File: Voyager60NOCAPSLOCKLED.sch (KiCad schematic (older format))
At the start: 262 parts, among them Q1 2N7002, SW1 5.2x5.2mm, U1 ATmega32U4-MU, U2 PRTR5V0U2X, Y1 16Mhz

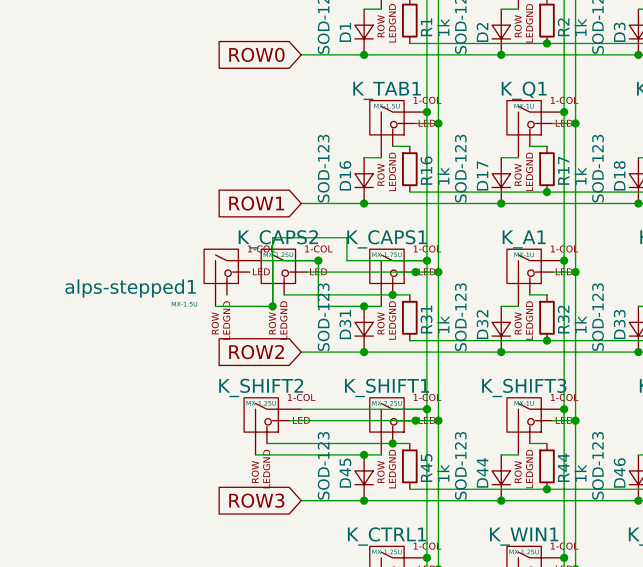
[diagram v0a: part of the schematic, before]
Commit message: Alps Stepped Caps Lock
Added alps stepped caps lock support at the cost of removing caps lock LED support.
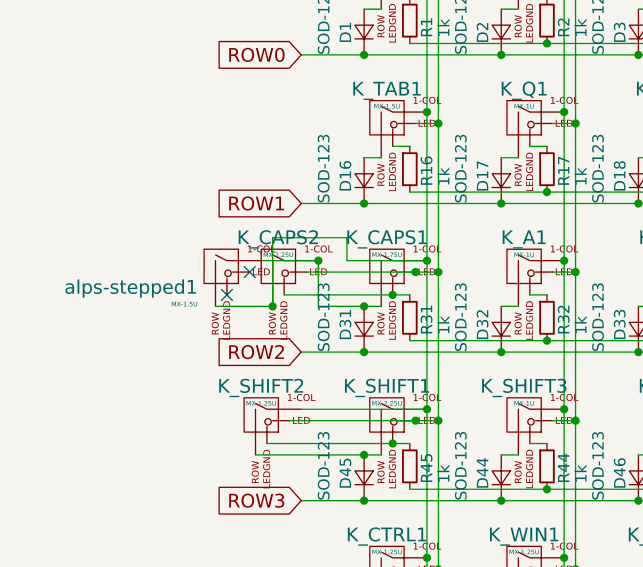
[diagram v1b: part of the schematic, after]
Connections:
- no-connect marks 2 -> 4
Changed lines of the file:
@@
 EESchema Schematic File Version 4
-LIBS:Voyager60-cache
+LIBS:Voyager60NOCAPSLOCKLED-cache
 EELAYER 26 0
 EELAYER END
@@
 	1125 2525 800  2525
 Wire Wire Line
-	800  2525 800  2825
-Wire Wire Line
 	1000 2625 1000 2825
 Connection ~ 1200 2825
@@
 $EndComp
 Wire Wire Line
+	550  2825 800  2825
+Connection ~ 800  2825
+NoConn ~ 600  2775
+NoConn ~ 700  2675
+Wire Wire Line
 	750  2625 1000 2625
 Connection ~ 1000 2625
 Wire Wire Line
-	550  2825 800  2825
-Connection ~ 800  2825
+	800  2525 800  2825
 $EndSCHEMATC
